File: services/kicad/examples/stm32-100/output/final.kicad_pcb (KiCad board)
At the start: 2 copper layers, 208 x 156 mm, 100 parts, among them J1 5V, U1 STM32F103C8T6, U2 AMS1117-3.3

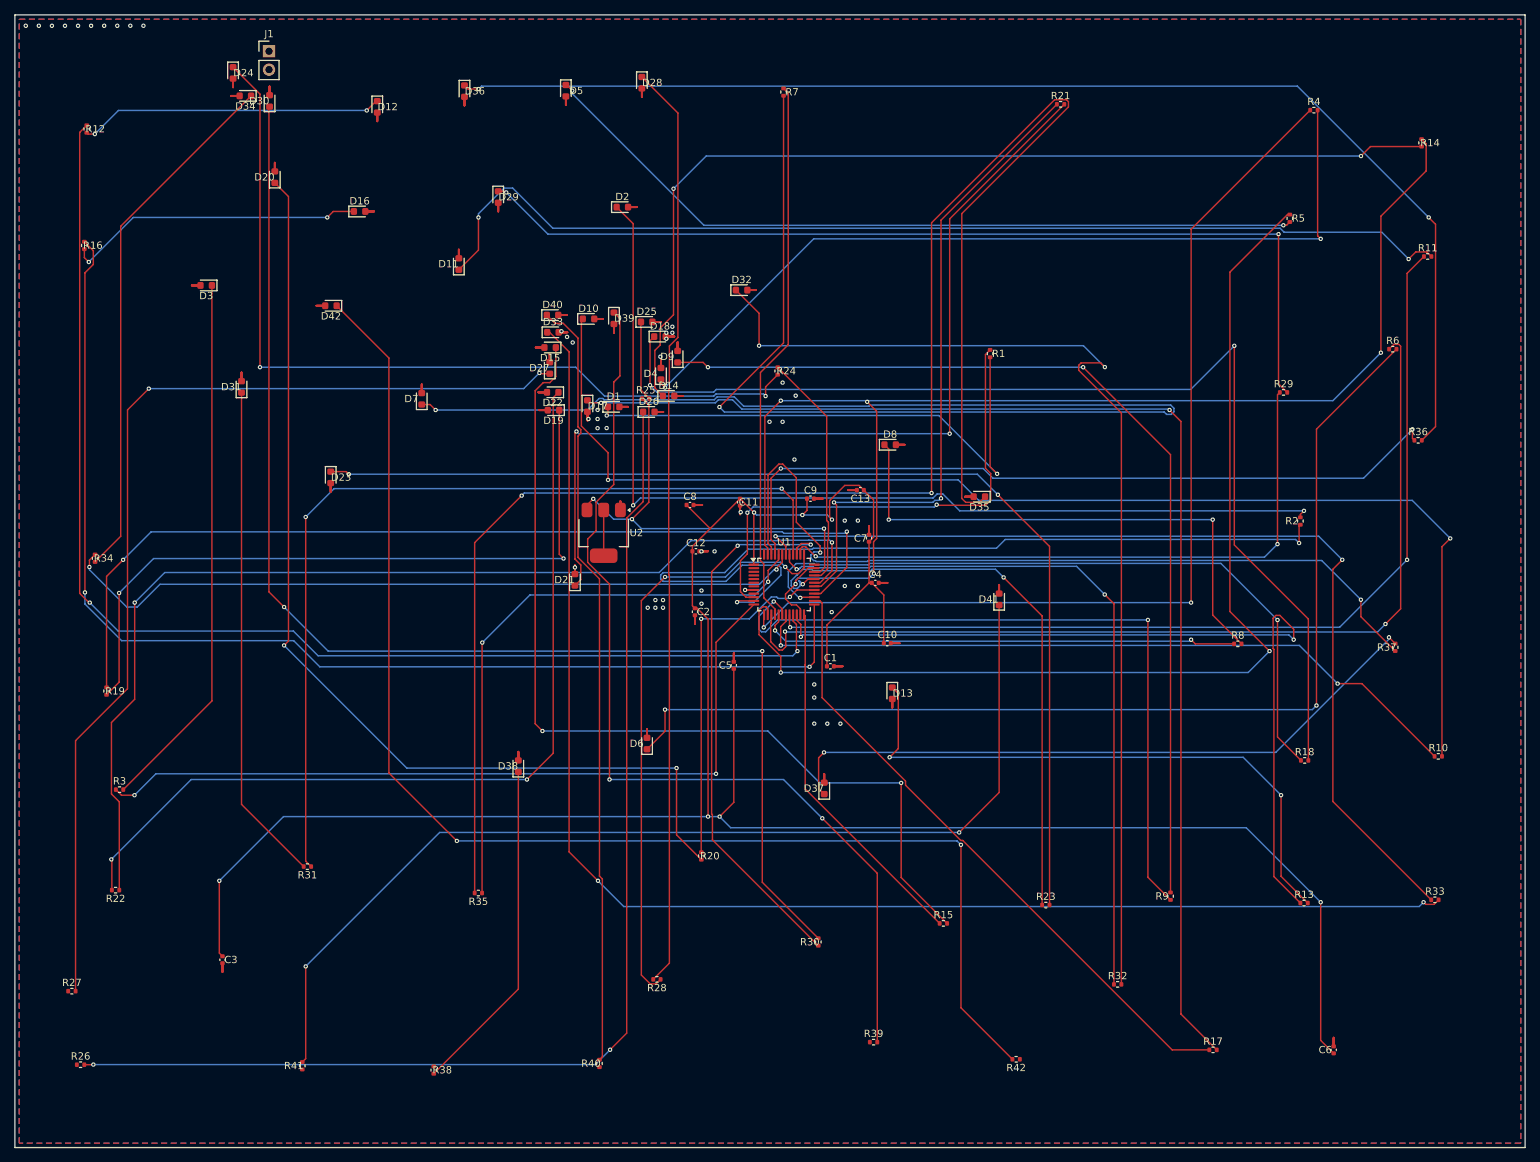
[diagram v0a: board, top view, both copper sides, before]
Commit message: feat(kicad): placement pro et routage 100 % fabricable sur les 16 cartes -- integration sur main (#164)
Branche d'integration coupee depuis origin/main (fab2a82, PR #162) : les
fichiers cles de main etaient des instantanes de feat/placement-seed-snap-
bypass (routing.py = 7981019, placement.py = 437a8b4...). On reprend donc
l'arbre entier de cette branche (345 commits, dernier 9f48667) et on y
conserve ce que main seul apportait :
- tools/verrou_routage.py + son test : « 6,2 Go par routage » rectifie
  (0,2 Go mesure ; c'est la concurrence qui emballe la memoire) ;
- tests/test_driver_llm_resync.py ;
- CLAUDE.md, PLAN.md, DECISIONS.md : fusion a trois voies, les sections
  des deux lignes conservees (2026-09-05 conteneur/verrou, 2026-09-07
  parcours asynchrone et chaine du driver, 2026-09-09/10 lecons).
Les skills *-delegate restent supprimes (remplaces le 2026-08-30).

Contenu : banc en deux phases (placement valide puis routage gele), snap
sur les regles natives, repli GND cible, journal Freerouting incremental,
horloge sans progres, via d'echappement vers le plan principal,
serigraphie degagee ; 16 cartes livrees a 100 %, 0 erreur DRC.

Verification : pytest services/kicad 1805 passed, 16 skipped ;
pnpm type-check 8/8.


Claude-Session: https://claude.ai/code/session_01TnMqm4La2CxQHHB5K8aSSV

Co-authored-by: Claude Fable 5.1 <noreply@anthropic.com>
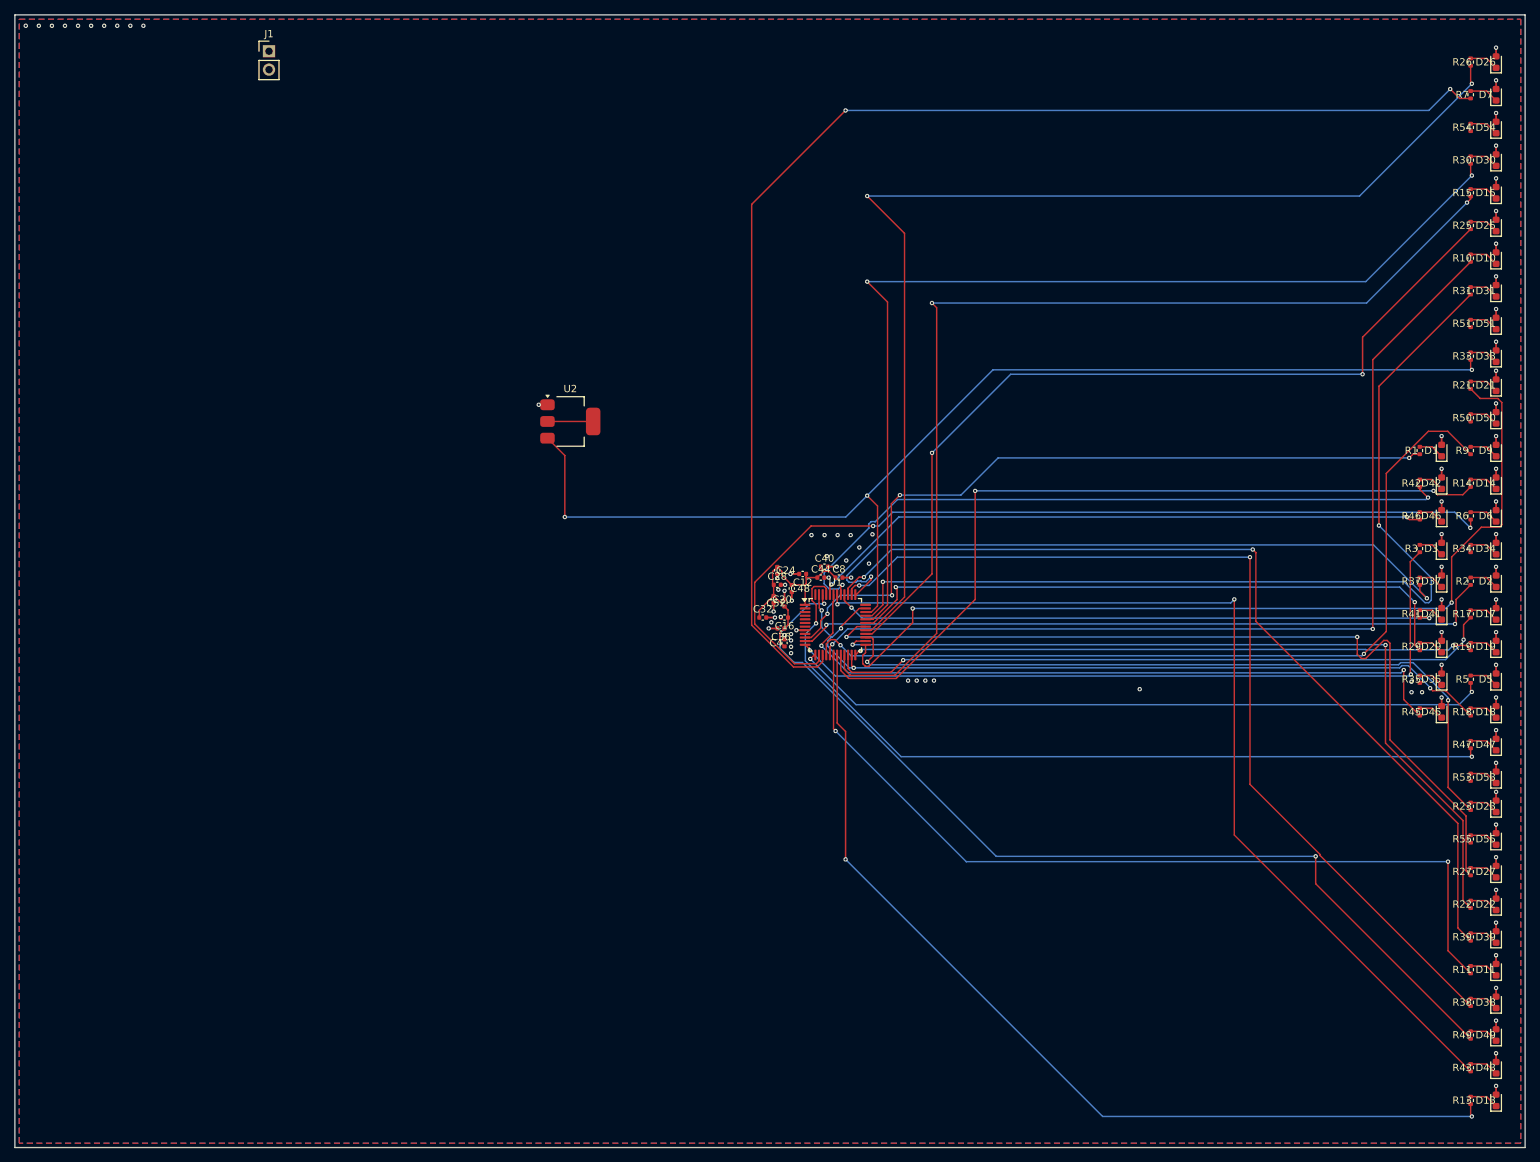
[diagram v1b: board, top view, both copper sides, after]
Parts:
- removed C1, C10, C11, C13, C2, C3, C5, C6, C7, C9: 100nF, C_0402_1005Metric
- removed D12, D16, D20, D24, D28, D32, D36, D4, D40, D8: LED, LED_0603_1608Metric
- removed R12, R16, R20, R24, R28, R32, R36, R4, R40, R8: 330, R_0402_1005Metric
- added C16: 100nF, C_0402_1005Metric, F.Cu at (150.5, 110.0)
- added C20: 100nF, C_0402_1005Metric, F.Cu at (149.0, 107.5)
- added C24: 100nF, C_0402_1005Metric, F.Cu at (149.5, 103.5)
- added C28: 100nF, C_0402_1005Metric, F.Cu at (149.5, 105.5)
- added C32: 100nF, C_0402_1005Metric, F.Cu at (147.5, 110.0)
- added C36: 100nF, C_0402_1005Metric, F.Cu at (150.0, 111.5)
- added C40: 100nF, C_0402_1005Metric, F.Cu at (156.0, 103.0)
- added C44: 100nF, C_0402_1005Metric, F.Cu at (155.5, 104.5)
- added C48: 100nF, C_0402_1005Metric, F.Cu at (151.5, 106.0)
- added C52: 100nF, C_0402_1005Metric, F.Cu at (150.5, 108.0)
- added D43: LED, LED_0603_1608Metric, F.Cu at (248.5, 172.0)
- added D45: LED, LED_0603_1608Metric, F.Cu at (241.0, 123.0)
- added D46: LED, LED_0603_1608Metric, F.Cu at (241.0, 96.0)
- added D47: LED, LED_0603_1608Metric, F.Cu at (248.5, 127.5)
- added D49: LED, LED_0603_1608Metric, F.Cu at (248.5, 167.5)
- added D50: LED, LED_0603_1608Metric, F.Cu at (248.5, 82.5)
- added D51: LED, LED_0603_1608Metric, F.Cu at (248.5, 69.5)
- added D53: LED, LED_0603_1608Metric, F.Cu at (248.5, 132.0)
- added D54: LED, LED_0603_1608Metric, F.Cu at (248.5, 42.5)
- added D55: LED, LED_0603_1608Metric, F.Cu at (248.5, 140.5)
- added R43: 330, R_0402_1005Metric, F.Cu at (245.0, 172.0)
- added R45: 330, R_0402_1005Metric, F.Cu at (238.0, 123.0)
- added R46: 330, R_0402_1005Metric, F.Cu at (238.0, 96.0)
- added R47: 330, R_0402_1005Metric, F.Cu at (245.0, 127.5)
- added R49: 330, R_0402_1005Metric, F.Cu at (245.0, 167.5)
- added R50: 330, R_0402_1005Metric, F.Cu at (245.0, 82.5)
- added R51: 330, R_0402_1005Metric, F.Cu at (245.0, 69.5)
- added R53: 330, R_0402_1005Metric, F.Cu at (245.0, 132.0)
- added R54: 330, R_0402_1005Metric, F.Cu at (245.0, 42.5)
- added R55: 330, R_0402_1005Metric, F.Cu at (245.0, 140.5)
- moved R26 236.1 mm to (245.0, 33.5), turned to 90 degrees
- moved R27 193.4 mm to (245.0, 145.0), turned to 90 degrees
- moved R34 189.5 mm to (245.0, 100.5), turned to 90 degrees
- moved R19 188.0 mm to (245.0, 114.0), turned to 90 degrees
- moved R22 186.6 mm to (245.0, 149.5), turned to 90 degrees
- moved D34 183.2 mm to (248.5, 100.5), turned to 90 degrees
- moved R3 182.1 mm to (238.0, 100.5), turned to 90 degrees
- moved R31 178.8 mm to (245.0, 65.0), turned to 90 degrees
- moved D3 174.0 mm to (241.0, 100.5), turned to 90 degrees
- moved D31 173.3 mm to (248.5, 65.0)
- moved D11 172.8 mm to (248.5, 158.5)
- moved D30 169.1 mm to (248.5, 47.0)
- moved D23 166.8 mm to (248.5, 136.0), turned to 90 degrees
- moved R41 166.0 mm to (238.0, 109.5)
- moved D42 154.9 mm to (241.0, 91.5), turned to 90 degrees
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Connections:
- D10 pad 1: LED13 -> LED10
- D11 pad 1: LED14 -> LED11
- D13 pad 1: LED17 -> LED13
- D14 pad 1: LED18 -> LED14
- D15 pad 1: LED19 -> LED15
- D17 pad 1: LED22 -> LED17
- D18 pad 1: LED23 -> LED18
- D19 pad 1: LED25 -> LED19
- D21 pad 1: LED27 -> LED21
- D22 pad 1: LED29 -> LED22
- D23 pad 1: LED30 -> LED23
- D25 pad 1: LED33 -> LED25
- D26 pad 1: LED34 -> LED26
- D27 pad 1: LED35 -> LED27
- D29 pad 1: LED38 -> LED29
- D30 pad 1: LED39 -> LED30
- D31 pad 1: LED41 -> LED31
- D33 pad 1: LED43 -> LED33
- D34 pad 1: LED45 -> LED34
- D35 pad 1: LED46 -> LED35
- D37 pad 1: LED49 -> LED37
- D38 pad 1: LED50 -> LED38
- D39 pad 1: LED51 -> LED39
- D41 pad 1: LED54 -> LED41
- D42 pad 1: LED55 -> LED42
- D5 pad 1: LED6 -> LED5
- D6 pad 1: LED7 -> LED6
- D7 pad 1: LED9 -> LED7
- D9 pad 1: LED11 -> LED9
- R10 pad 1: GPIO13 -> GPIO10
- R10 pad 2: LED13 -> LED10
- R11 pad 1: GPIO14 -> GPIO11
- R11 pad 2: LED14 -> LED11
- R13 pad 1: GPIO17 -> GPIO13
- R13 pad 2: LED17 -> LED13
- R14 pad 1: GPIO18 -> GPIO14
- R14 pad 2: LED18 -> LED14
- R15 pad 1: GPIO19 -> GPIO15
- R15 pad 2: LED19 -> LED15
- R17 pad 1: GPIO22 -> GPIO17
- R17 pad 2: LED22 -> LED17
- R18 pad 1: GPIO23 -> GPIO18
- R18 pad 2: LED23 -> LED18
- R19 pad 1: GPIO25 -> GPIO19
- R19 pad 2: LED25 -> LED19
- R21 pad 1: GPIO27 -> GPIO21
- R21 pad 2: LED27 -> LED21
- R22 pad 1: GPIO29 -> GPIO22
- R22 pad 2: LED29 -> LED22
- R23 pad 1: GPIO30 -> GPIO23
- R23 pad 2: LED30 -> LED23
- R25 pad 1: GPIO33 -> GPIO25
- R25 pad 2: LED33 -> LED25
- R26 pad 1: GPIO34 -> GPIO26
- R26 pad 2: LED34 -> LED26
- R27 pad 1: GPIO35 -> GPIO27
- R27 pad 2: LED35 -> LED27
- R29 pad 1: GPIO38 -> GPIO29
- R29 pad 2: LED38 -> LED29
- R30 pad 1: GPIO39 -> GPIO30
- R30 pad 2: LED39 -> LED30
- R31 pad 1: GPIO41 -> GPIO31
- R31 pad 2: LED41 -> LED31
- R33 pad 1: GPIO43 -> GPIO33
- R33 pad 2: LED43 -> LED33
- R34 pad 1: GPIO45 -> GPIO34
- R34 pad 2: LED45 -> LED34
- R35 pad 1: GPIO46 -> GPIO35
- R35 pad 2: LED46 -> LED35
- R37 pad 1: GPIO49 -> GPIO37
- R37 pad 2: LED49 -> LED37
- R38 pad 1: GPIO50 -> GPIO38
- R38 pad 2: LED50 -> LED38
- R39 pad 1: GPIO51 -> GPIO39
- R39 pad 2: LED51 -> LED39
- R41 pad 1: GPIO54 -> GPIO41
- R41 pad 2: LED54 -> LED41
- R42 pad 1: GPIO55 -> GPIO42
- R42 pad 2: LED55 -> LED42
- R5 pad 1: GPIO6 -> GPIO5
- R5 pad 2: LED6 -> LED5
- R6 pad 1: GPIO7 -> GPIO6
- R6 pad 2: LED7 -> LED6
- R7 pad 1: GPIO9 -> GPIO7
- R7 pad 2: LED9 -> LED7
- R9 pad 1: GPIO11 -> GPIO9
- R9 pad 2: LED11 -> LED9
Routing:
- net +3V3: track 334.7 -> 31.7 mm, vias 7 -> 0
- net LED46: track 241.7 -> 3.54 mm, vias 2 -> 0
- net LED9: track 215.8 -> 4.04 mm, vias 2 -> 0
- net GND: track 273.6 -> 64.8 mm, vias 50 -> 90
- net LED43: track 196.5 -> 4.04 mm, vias 2 -> 0
- net LED55: track 182.7 -> 4.04 mm, vias 2 -> 0
- net LED39: track 180.9 -> 4.04 mm, vias 2 -> 0
- net LED13: track 173.6 -> 4.04 mm, vias 2 -> 0
- net LED47: track 172.5 -> 4.04 mm, vias 2 -> 0
- net LED22: track 171.9 -> 4.04 mm, vias 2 -> 0
- net LED34: track 163.0 -> 4.04 mm, vias 2 -> 0
- net LED30: track 152.7 -> 4.04 mm, vias 2 -> 0
- net LED23: track 151.8 -> 4.04 mm, vias 2 -> 0
- net LED7: track 150.1 -> 4.04 mm, vias 2 -> 0
- net LED42: track 149.5 -> 3.54 mm, vias 2 -> 0
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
